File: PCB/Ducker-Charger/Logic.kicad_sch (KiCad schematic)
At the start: 0 parts

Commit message: feat: begun Logic
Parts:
- added C10, C11, C12, C13, C9: 10n, symbol Device:C
- added C14: 100n, symbol Device:C
- added J3: SWDEBUG_CONN, Connector_IDC:IDC-Header_2x05_P2.54mm_Vertical, symbol Eagle_Main:SWDEBUG_CONN
- added R8, R9: 10, symbol Device:R
- added U2: STM32F401RBT6, EasyEDA:LQFP-64_L10.0-W10.0-P0.50-LS12.0-BL, symbol EasyEDA:STM32F401RBT6
- added U3: INA226AIDGSR, EasyEDA:MSOP-10_L3.0-W3.0-P0.50-LS5.0-BL, symbol EasyEDA:INA226AIDGSR
- added Y1: 8MHz, symbol Device:Crystal_GND24
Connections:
- new net: C14.1, R8.2
- new net: C14.2, R9.2
- new net: R8.1, U3.10 (VIN+)
- new net: R9.1, U3.9 (VIN-)
- new net +3V3: C10.1, C11.1, C12.1, C13.1, C9.1
- new net GND: C10.2, C11.2, C12.2, C13.2, C9.2, U3.1 (A1), U3.2 (A0)

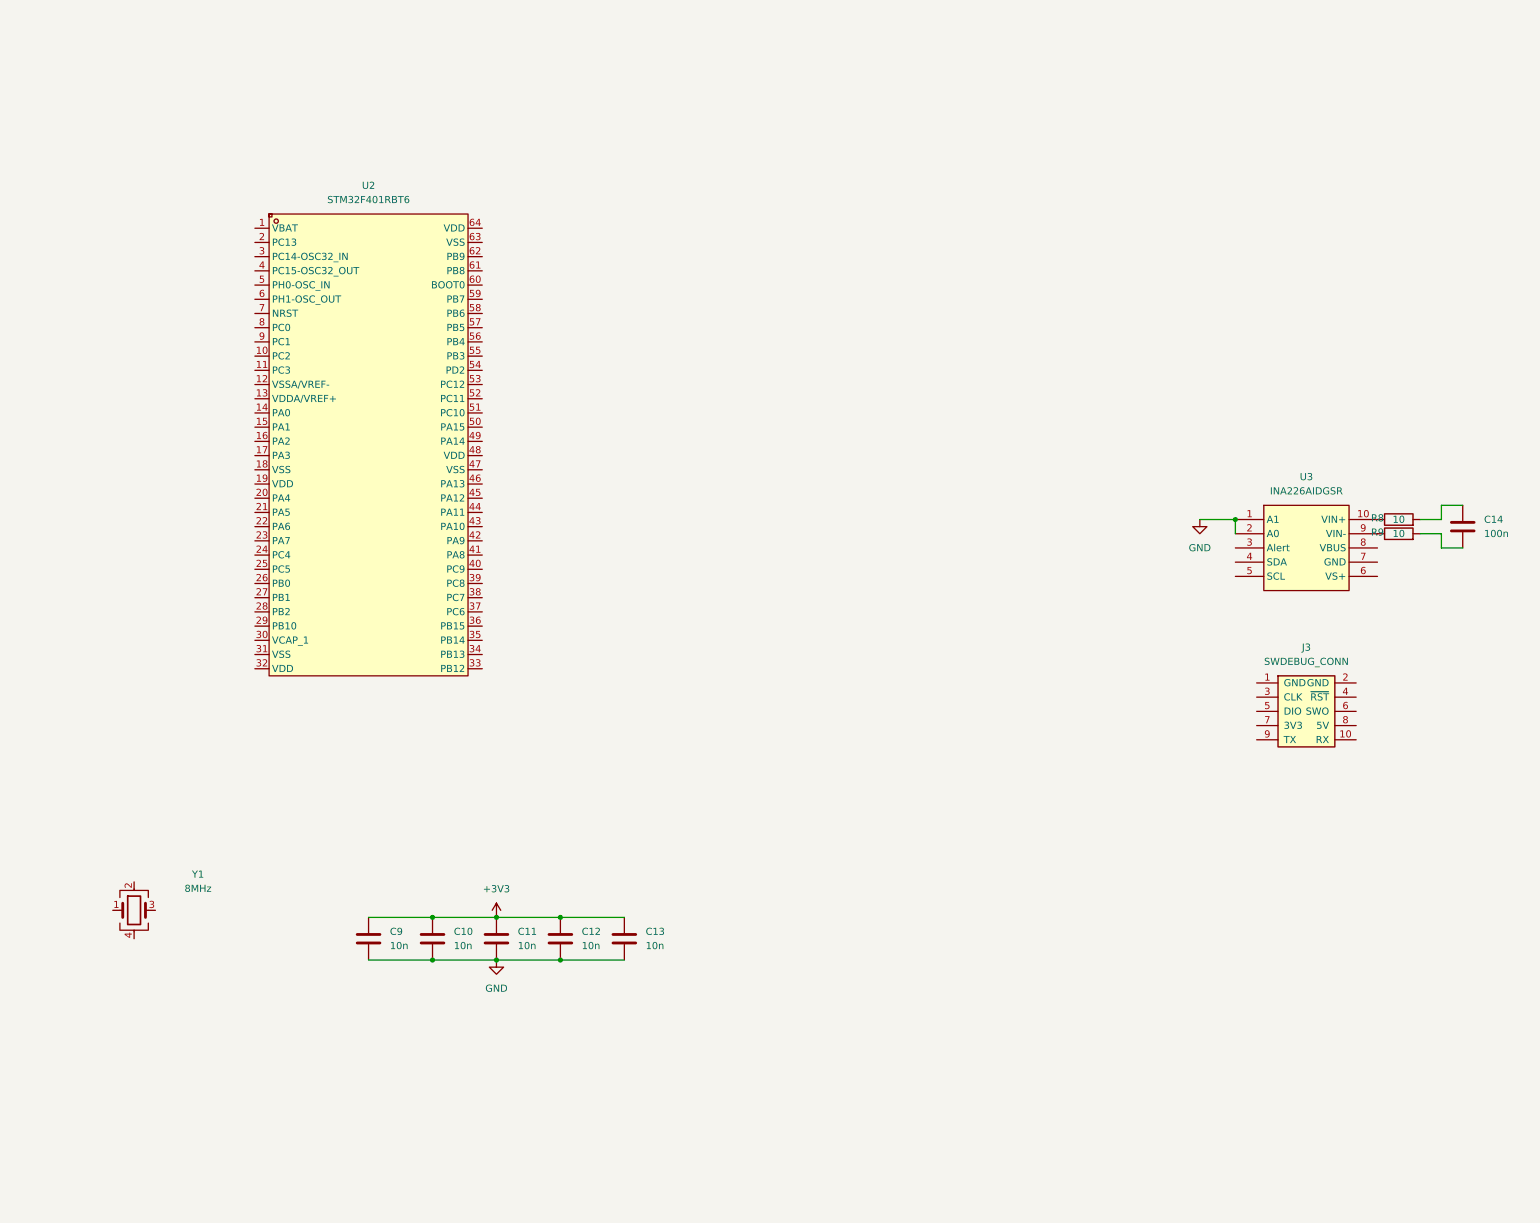
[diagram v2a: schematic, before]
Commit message: feat: progressed MCU setup, completed 3V3 voltage regulator
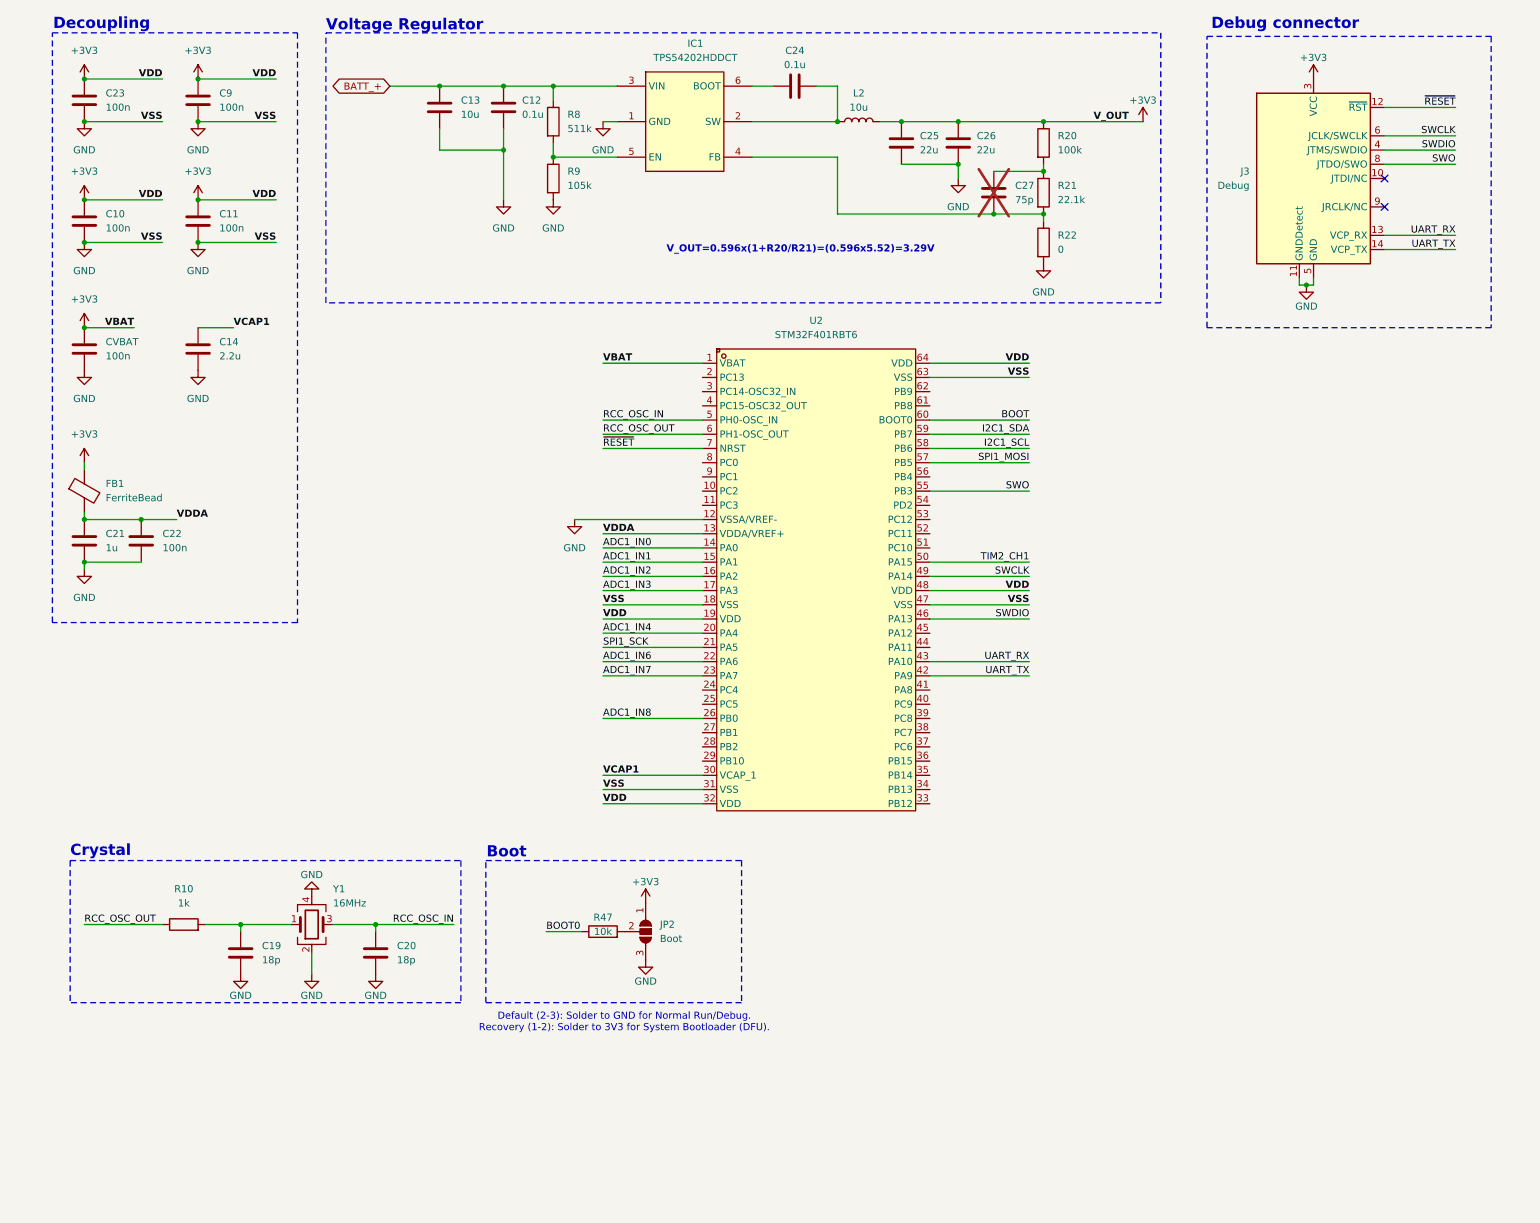
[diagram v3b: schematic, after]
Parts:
- removed J3: SWDEBUG_CONN, Connector_IDC:IDC-Header_2x05_P2.54mm_Vertical, symbol Eagle_Main:SWDEBUG_CONN
- removed U3: INA226AIDGSR, EasyEDA:MSOP-10_L3.0-W3.0-P0.50-LS5.0-BL, symbol EasyEDA:INA226AIDGSR
- added C19, C20: 18p, Capacitor_SMD:C_0603_1608Metric, symbol Device:C
- added C21: 1u, symbol Device:C
- added C22, C23, CVBAT: 100n, symbol Device:C
- added C24: 0.1u, symbol Device:C
- added C25, C26: 22u, symbol Device:C
- added C27: 75p, symbol Device:C
- added FB1: FerriteBead, symbol Device:FerriteBead
- added IC1: TPS54202HDDCT, SOT95P280X110-6N, symbol TPS54202HDDCT:TPS54202HDDCT
- added J3: Debug, Eagle_Connectors:SAMTEC_FTSH-107-01-L-DV-K-TR, symbol Connector:Conn_ST_STDC14
- added JP2: Boot, Jumper:SolderJumper-3_P1.3mm_Open_RoundedPad1.0x1.5mm, symbol Jumper:SolderJumper_3_Open
- added L2: 10u, symbol Device:L
- added R10: 1k, Resistor_SMD:R_0603_1608Metric, symbol Device:R
- added R20: 100k, symbol Device:R
- added R21: 22.1k, symbol Device:R
- added R22: 0, symbol Device:R
- added R47: 10k, Resistor_SMD:R_0603_1608Metric, symbol Device:R
- C10, C11, C9: value 10n -> 100n
- C12: value 10n -> 0.1u
- C13: value 10n -> 10u
- C14: value 100n -> 2.2u
- R8: value 10 -> 511k
- R9: value 10 -> 105k
- Y1: value 8MHz -> 16MHz; footprint (none) -> Crystal:Crystal_SMD_EuroQuartz_MT-4Pin_3.2x2.5mm
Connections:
- net +3V3: now also U2.1 (VBAT), U2.19 (VDD), U2.32 (VDD), U2.48 (VDD), U2.64 (VDD), C23.1, C25.1, C26.1, CVBAT.1, FB1.1, J3.3 (VCC), JP2.1 (A), L2.2, R20.1; no longer C12.1, C13.1
- net GND: now also C14.2, R9.2, U2.12 (VSSA/VREF-), U2.18 (VSS), U2.31 (VSS), U2.47 (VSS), U2.63 (VSS), Y1.2, Y1.4, C19.2, C20.2, C21.2, C22.2, C23.2, C25.2, C26.2, CVBAT.2, IC1.1 (GND), J3.11 (GNDDetect), J3.5 (GND), J3.7 (GND), JP2.3 (B), R22.2
- net at R8.2: now also R9.1, IC1.5 (EN); no longer C14.1
- net BATT_+: now reaches R8.1
- net BATT_+: now also C12.1, C13.1, IC1.3 (VIN)
- net at Y1.1: now also C19.1, R10.2
- net RCC_OSC_IN: now reaches Y1.3
- net RCC_OSC_IN: now also U2.5 (PH0-OSC_IN), C20.1
- net VDDA: now reaches U2.13 (VDDA/VREF+)
- net VDDA: now also C21.1, C22.1, FB1.2
- net ADC1_IN0: now reaches U2.14 (PA0)
- net ADC1_IN1: now reaches U2.15 (PA1)
- net ADC1_IN2: now reaches U2.16 (PA2)
- net ADC1_IN3: now reaches U2.17 (PA3)
- net ADC1_IN4: now reaches U2.20 (PA4)
- net SPI1_SCK: now reaches U2.21 (PA5)
- net ADC1_IN6: now reaches U2.22 (PA6)
- net ADC1_IN7: now reaches U2.23 (PA7)
- net ADC1_IN8: now reaches U2.26 (PB0)
- net VCAP1: now reaches U2.30 (VCAP_1)
- net VCAP1: now also C14.1
- net UART_TX: now reaches U2.42 (PA9)
- net UART_TX: now also J3.14 (VCP_TX)
- net UART_RX: now reaches U2.43 (PA10)
- net UART_RX: now also J3.13 (VCP_RX)
- net SWDIO: now reaches U2.46 (PA13)
- net SWDIO: now also J3.4 (JTMS/SWDIO)
- net SWCLK: now reaches U2.49 (PA14)
- net SWCLK: now also J3.6 (JCLK/SWCLK)
- net TIM2_CH1: now reaches U2.50 (PA15)
- net SWO: now reaches U2.55 (PB3)
- net SWO: now also J3.8 (JTDO/SWO)
- net SPI1_MOSI: now reaches U2.57 (PB5)
- net I2C1_SCL: now reaches U2.58 (PB6)
- net I2C1_SDA: now reaches U2.59 (PB7)
- net RCC_OSC_OUT: now reaches U2.6 (PH1-OSC_OUT)
- net RCC_OSC_OUT: now also R10.1
- net BOOT: now reaches U2.60 (BOOT0)
- net ~{RESET}: now reaches U2.7 (NRST)
- net ~{RESET}: now also J3.12 (~{RST})
- new net: JP2.2 (C), R47.2
- new net: C27.2, R20.2, R21.1
- new net: C27.1, IC1.4 (FB), R21.2, R22.1
- new net: C24.2, IC1.2 (SW), L2.1
- new net: C24.1, IC1.6 (BOOT)
- new net BOOT0: R47.1
- no-connect marks 0 -> 2
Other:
- note added: "Boot"
- note added: "Crystal"
- note added: "Debug connector"
- note added: "Decoupling"
- note added: "Default (2-3): Solder to GND for Normal Run/Debug. Recovery (1-2): Solder to 3V3 for System Bootloader (DFU)."
- note added: "V_OUT=0.596x(1+R20/R21)=(0.596x5.52)=3.29V"
- note added: "Voltage Regulator"
- moved on the sheet: U2

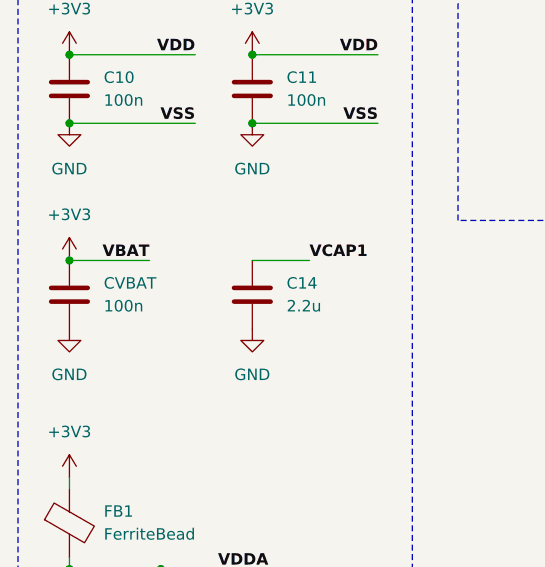
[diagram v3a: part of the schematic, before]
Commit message: fix: placement and values
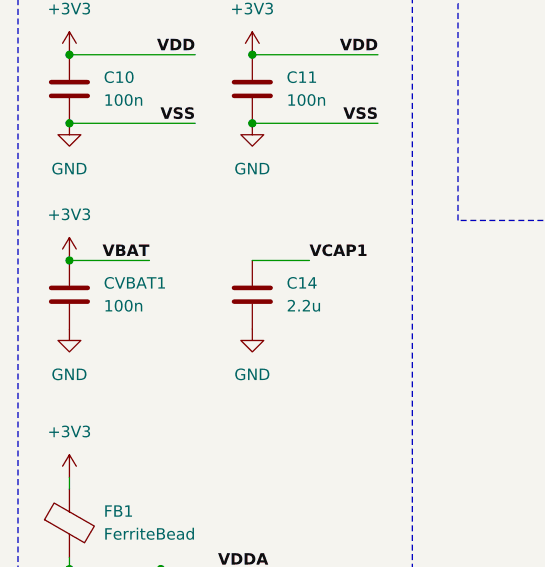
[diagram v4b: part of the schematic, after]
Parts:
- renumbered CVBAT to CVBAT1
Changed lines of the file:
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@@
 		(dnp no)
 		(fields_autoplaced yes)
-		(property "Reference" "CVBAT"
+		(property "Reference" "CVBAT1"
 			(at 27.94 73.6599 0)
 			(effects
@@
 			(project "Ducker-Charger"
 				(path "/74790d6c-a68e-4e6d-b4a9-43de1843f817/b1375a06-d47d-478c-835c-6ba88db99bcf"
-					(reference "CVBAT")
+					(reference "CVBAT1")
 					(unit 1)
 				)

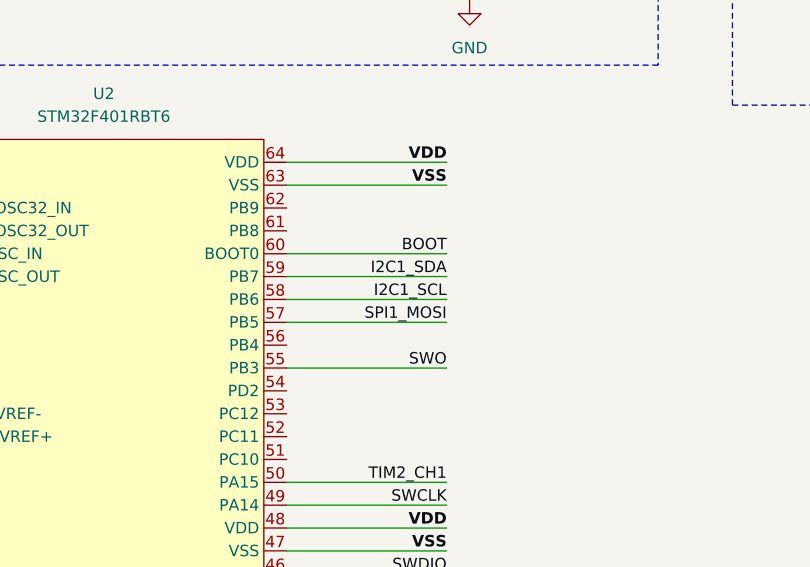
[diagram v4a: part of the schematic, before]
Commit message: feat: added pullup resistors for i2c
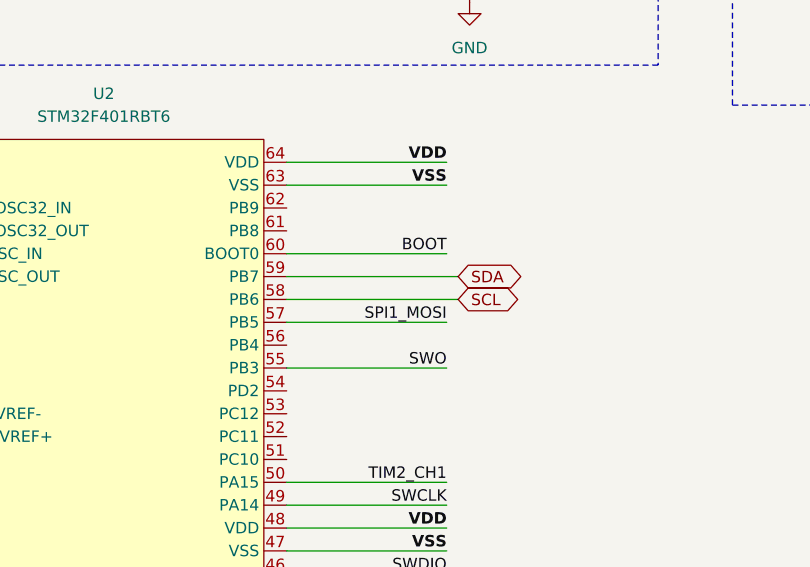
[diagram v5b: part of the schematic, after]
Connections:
- net I2C1_SCL renamed SCL
- net I2C1_SDA renamed SDA
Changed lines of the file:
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@@
+	(wire
+		(pts
+			(xy 194.31 90.17) (xy 175.26 90.17)
+		)
+		(stroke
+			(width 0)
+			(type default)
+		)
+	)
 	(wire
 		(pts
@@
 	(wire
 		(pts
+			(xy 194.31 92.71) (xy 175.26 92.71)
+		)
+		(stroke
+			(width 0)
+			(type default)
+		)
+	)
+	(wire
+		(pts
 			(xy 116.84 90.17) (xy 134.62 90.17)
 		)
@@
 	(wire
 		(pts
-			(xy 175.26 92.71) (xy 193.04 92.71)
-		)
-		(stroke
-			(width 0)
-			(type default)
-		)
-	)
-	(wire
-		(pts
 			(xy 116.84 128.27) (xy 134.62 128.27)
 		)
@@
 		(pts
 			(xy 193.04 118.11) (xy 175.26 118.11)
-		)
-		(stroke
-			(width 0)
-			(type default)
-		)
-	)
-	(wire
-		(pts
-			(xy 175.26 90.17) (xy 193.04 90.17)
 		)
 		(stroke
@@
 		)
 	)
-	(label "I2C1_SDA"
-		(at 193.04 90.17 180)
-		(effects
-			(font
-				(size 1.27 1.27)
-				(thickness 0.1588)
-			)
-			(justify right bottom)
-		)
-	)
 	(label "VSS"
 		(at 116.84 120.65 0)
@@
 		)
 	)
-	(label "I2C1_SCL"
-		(at 193.04 92.71 180)
-		(effects
-			(font
-				(size 1.27 1.27)
-				(thickness 0.1588)
-			)
-			(justify right bottom)
-		)
-	)
 	(label "SWCLK"
 		(at 269.24 36.83 180)
@@
 		)
 	)
+	(global_label "SDA"
+		(shape bidirectional)
+		(at 194.31 90.17 0)
+		(fields_autoplaced yes)
+		(effects
+			(font
+				(size 1.27 1.27)
+				(thickness 0.1588)
+			)
+			(justify left)
+		)
+		(property "Intersheetrefs" "${INTERSHEET_REFS}"
+			(at 201.9746 90.17 0)
+			(effects
+				(font
+					(size 1.27 1.27)
+				)
+				(justify left)
+				(hide yes)
+			)
+		)
+	)
+	(global_label "SCL"
+		(shape bidirectional)
+		(at 194.31 92.71 0)
+		(fields_autoplaced yes)
+		(effects
+			(font
+				(size 1.27 1.27)
+				(thickness 0.1588)
+			)
+			(justify left)
+		)
+		(property "Intersheetrefs" "${INTERSHEET_REFS}"
+			(at 201.9141 92.71 0)
+			(effects
+				(font
+					(size 1.27 1.27)
+				)
+				(justify left)
+				(hide yes)
+			)
+		)
+	)
